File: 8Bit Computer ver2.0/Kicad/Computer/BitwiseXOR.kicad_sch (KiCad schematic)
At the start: 5 parts, among them IC17 SN74LVC1G14DBVR, IC5 SN74AHC86DR, IC63 SN74AHC74DR, IC64 SN74ABT574ADWR, IC9 SN74AHC86DR

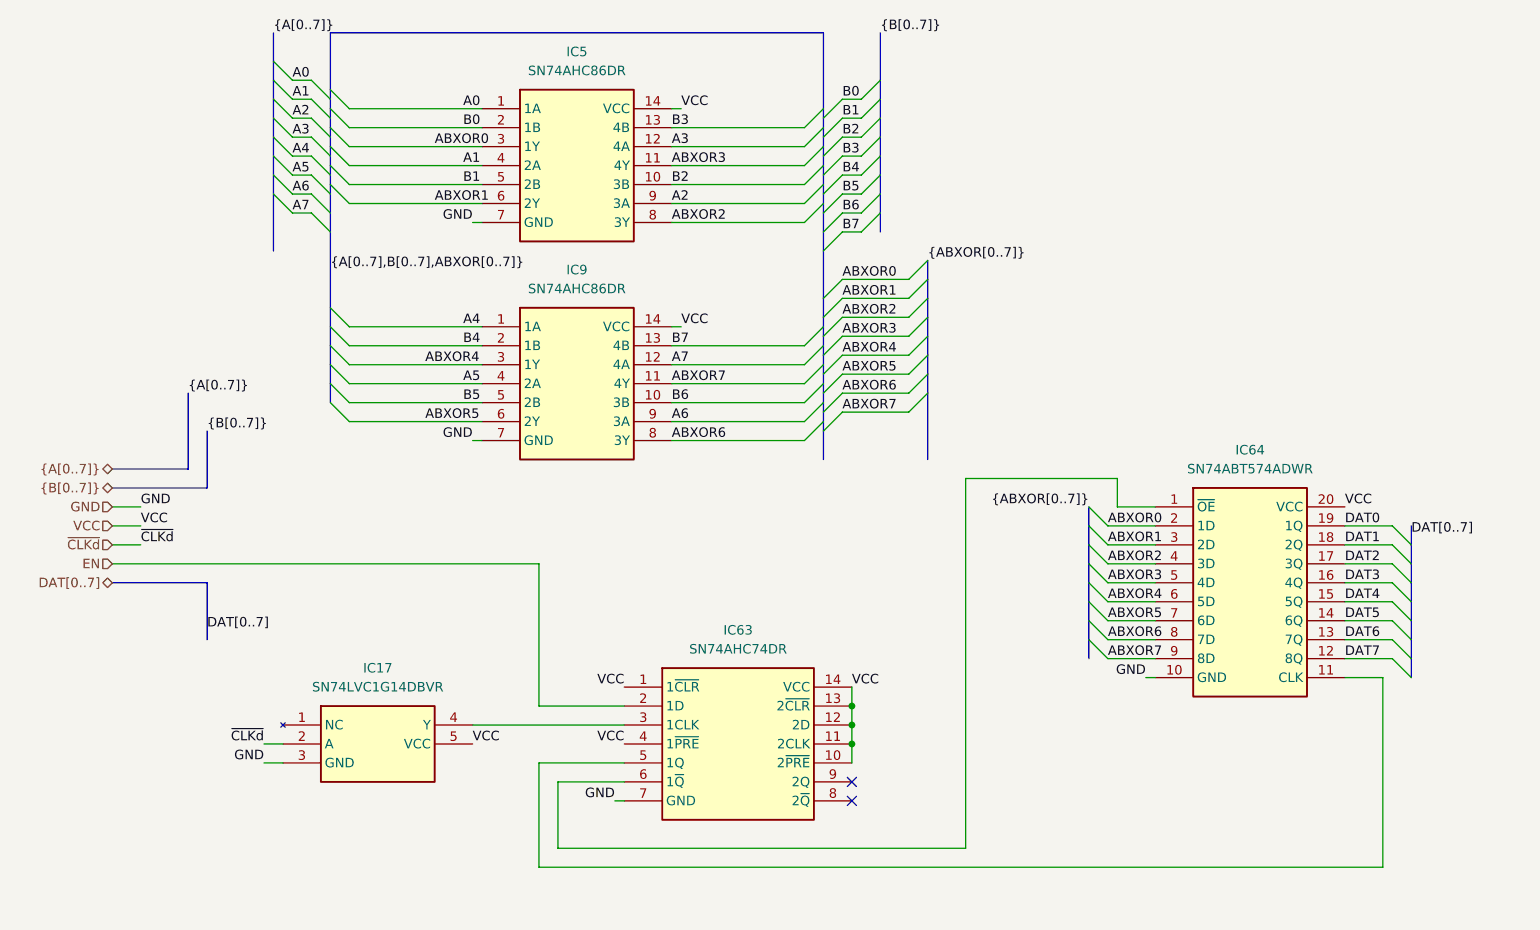
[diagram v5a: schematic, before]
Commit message: Kicad SCH/PCB
Kicad SCH/PCB:
changed the References in SCH
began with INOUTPUT module nearly done
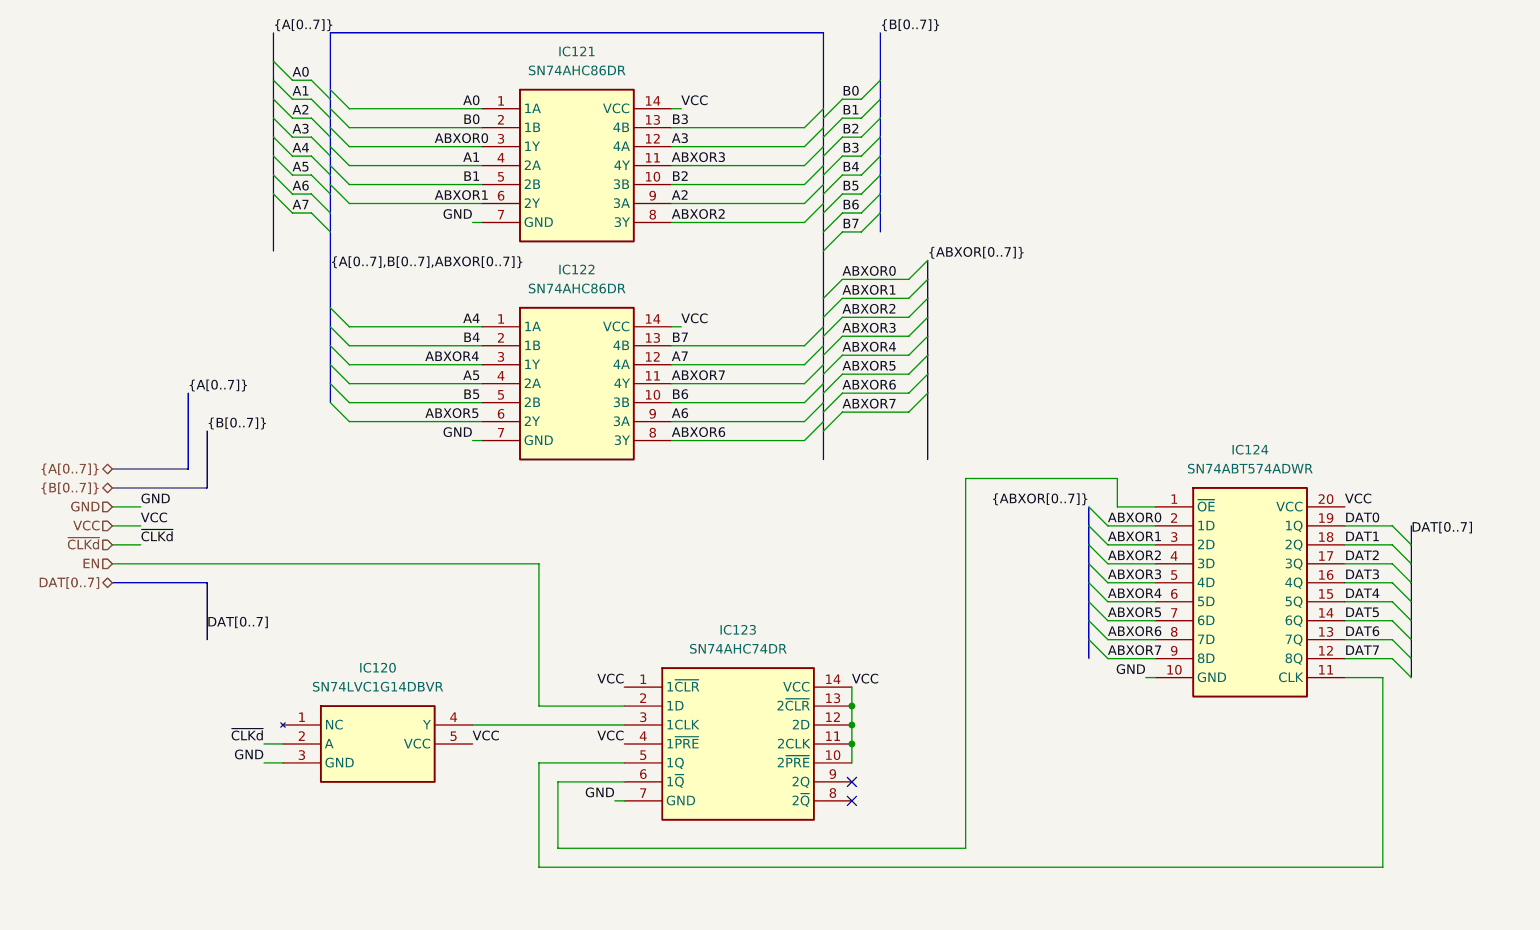
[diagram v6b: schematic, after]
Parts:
- renumbered IC17 to IC120, IC5 to IC121, IC9 to IC122, IC63 to IC123, IC64 to IC124
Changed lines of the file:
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@@
 		(dnp no)
 		(fields_autoplaced yes)
-		(property "Reference" "IC5"
+		(property "Reference" "IC121"
 			(at 109.22 33.02 0)
 			(effects
@@
 			(project "Computer"
 				(path "/1196a00e-6878-4d6d-82b7-9e052dfe7c14/c4d8b530-1c6d-45af-88d2-7dc1d4321a34/b731a2c3-fa27-45d9-a37d-42ef1ac61baf"
-					(reference "IC5")
+					(reference "IC121")
 					(unit 1)
 				)
@@
 		(dnp no)
 		(fields_autoplaced yes)
-		(property "Reference" "IC63"
+		(property "Reference" "IC123"
 			(at 130.81 110.49 0)
 			(effects
@@
 			(project "Computer"
 				(path "/1196a00e-6878-4d6d-82b7-9e052dfe7c14/c4d8b530-1c6d-45af-88d2-7dc1d4321a34/b731a2c3-fa27-45d9-a37d-42ef1ac61baf"
-					(reference "IC63")
+					(reference "IC123")
 					(unit 1)
 				)
@@
 		(dnp no)
 		(fields_autoplaced yes)
-		(property "Reference" "IC64"
+		(property "Reference" "IC124"
 			(at 199.39 86.36 0)
 			(effects
@@
 			(project "Computer"
 				(path "/1196a00e-6878-4d6d-82b7-9e052dfe7c14/c4d8b530-1c6d-45af-88d2-7dc1d4321a34/b731a2c3-fa27-45d9-a37d-42ef1ac61baf"
-					(reference "IC64")
+					(reference "IC124")
 					(unit 1)
 				)
@@
 		(dnp no)
 		(fields_autoplaced yes)
-		(property "Reference" "IC17"
+		(property "Reference" "IC120"
 			(at 82.55 115.57 0)
 			(effects
@@
 			(project "Computer"
 				(path "/1196a00e-6878-4d6d-82b7-9e052dfe7c14/c4d8b530-1c6d-45af-88d2-7dc1d4321a34/b731a2c3-fa27-45d9-a37d-42ef1ac61baf"
-					(reference "IC17")
+					(reference "IC120")
 					(unit 1)
 				)
@@
 		(dnp no)
 		(fields_autoplaced yes)
-		(property "Reference" "IC9"
+		(property "Reference" "IC122"
 			(at 109.22 62.23 0)
 			(effects
@@
 			(project "Computer"
 				(path "/1196a00e-6878-4d6d-82b7-9e052dfe7c14/c4d8b530-1c6d-45af-88d2-7dc1d4321a34/b731a2c3-fa27-45d9-a37d-42ef1ac61baf"
-					(reference "IC9")
+					(reference "IC122")
 					(unit 1)
 				)

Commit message: changed page numbers, compressed ROOT file from A1 to A4
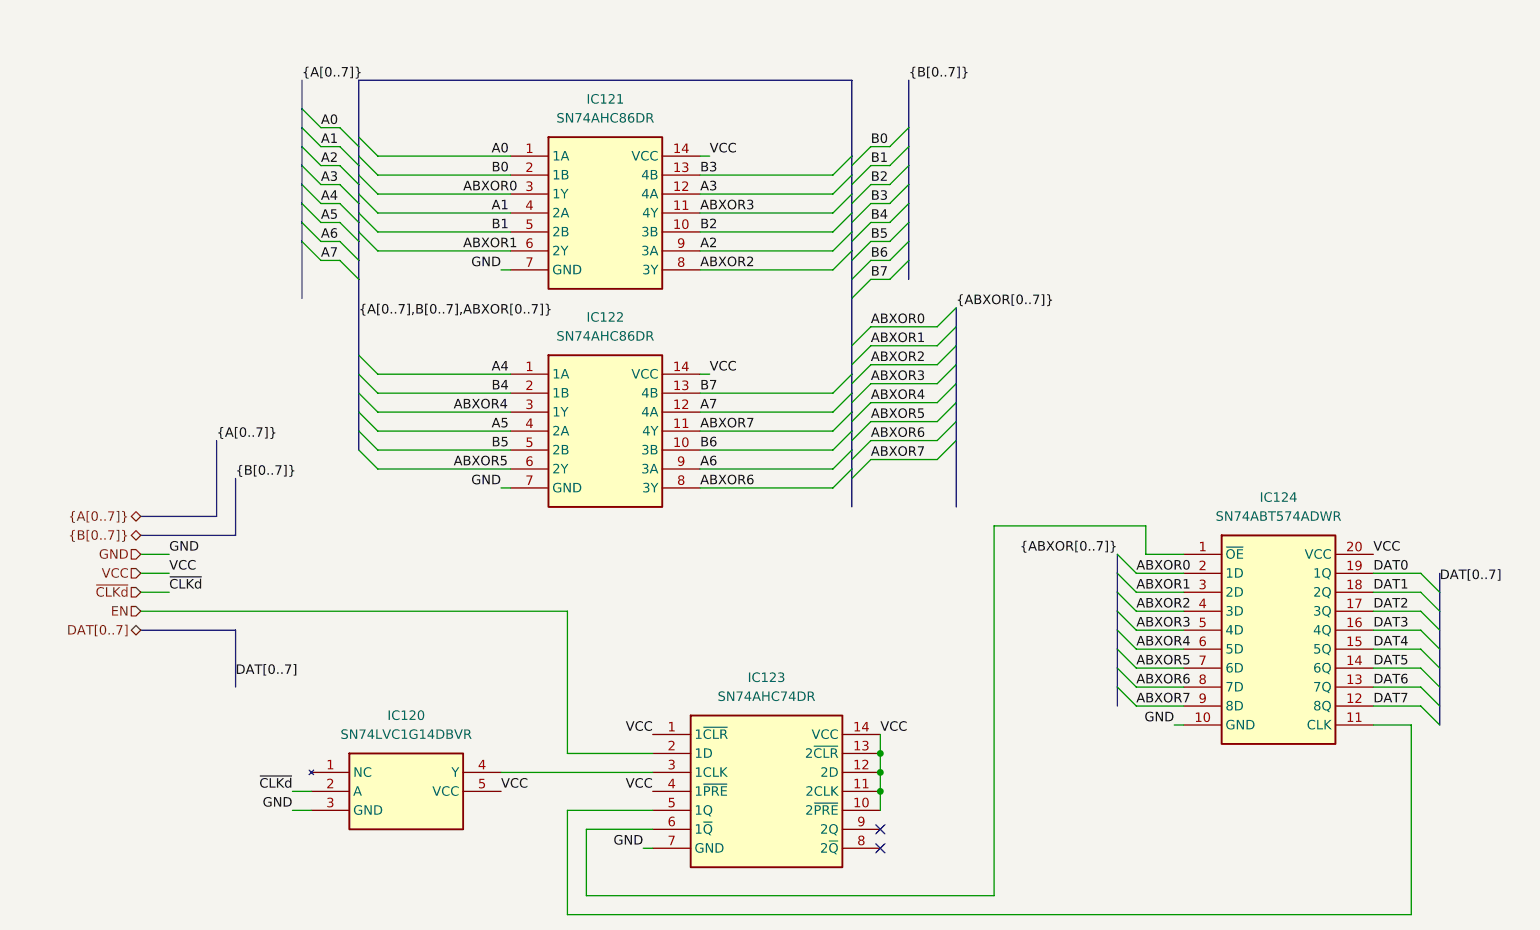
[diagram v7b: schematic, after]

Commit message: changed page numbers, every schematic is now A4
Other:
- title: (none) -> ${SHEETNAME}
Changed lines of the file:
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@@
 	(generator_version "9.0")
 	(paper "A4")
+	(title_block
+		(title "${SHEETNAME}")
+		(date "2026-03-21")
+		(rev "2.7")
+	)
 	(junction
 		(at 149.86 129.54)
